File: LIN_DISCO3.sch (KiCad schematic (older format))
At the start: 4 parts

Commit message: schematic: draft
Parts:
- added C1: 100nF, Capacitor_SMD:C_0805_2012Metric_Pad1.15x1.40mm_HandSolder, symbol Device:C
- added C4: CP, Capacitor_SMD:CP_Elec_4x5.8, symbol Device:CP
- added D1, D2: D_Zener_5V6, Diode_SMD:D_0805_2012Metric_Pad1.15x1.40mm_HandSolder, symbol Device:D_Zener
- added D3: LED, LED_SMD:LED_0805_2012Metric_Pad1.15x1.40mm_HandSolder, symbol Device:LED
- added J1: CAR_STAT, TerminalBlock:TerminalBlock_Altech_AK300-2_P5.00mm, symbol Connector:Conn_01x02_Female
- added J2: CAR_BAT, TerminalBlock:TerminalBlock_Altech_AK300-2_P5.00mm, symbol Connector:Conn_01x02_Female
- added J3: WEBASTO, TerminalBlock:TerminalBlock_Altech_AK300-2_P5.00mm, symbol Connector:Conn_01x02_Female
- added R1, R2, R3, R4: 10k, Resistor_SMD:R_0805_2012Metric_Pad1.15x1.40mm_HandSolder, symbol Device:R
- added R5: 2K, Resistor_SMD:R_0805_2012Metric_Pad1.15x1.40mm_HandSolder, symbol Device:R
- added R6: 1K, Resistor_SMD:R_0805_2012Metric_Pad1.15x1.40mm_HandSolder, symbol Device:R
- added U2: MCP1804x-5002xMB, Package_TO_SOT_SMD:SOT-89-3, symbol Regulator_Linear:MCP1804x-5002xMB
- added U3: Si9243A, Package_SO:SOIC-8_3.9x4.9mm_P1.27mm, symbol vishay_Si9243A:Si9243A
- C2, C3: renamed from C?; value C -> 22pF; footprint (none) -> Capacitor_SMD:C_0805_2012Metric_Pad1.15x1.40mm_HandSolder
- Rez1: renamed from Y?; value Crystal -> 18.432MHz; footprint (none) -> Crystal:Crystal_SMD_0603-2Pin_6.0x3.5mm_HandSoldering
- U1: renamed from U?; footprint (none) -> Package_SO:SOIC-18W_7.5x11.6mm_P1.27mm
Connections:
- net GND: now also C1.2, C4.2, D1.2 (A), D2.2 (A), J2.1 (Pin_1), R3.2, R4.2, U2.2 (GND), U3.5 (Gnd)
- net IGNITION: now also D1.1 (K), R2.1, R3.1
- net LOW_BEAM: now also D2.1 (K), R1.1, R4.1
- net Vcc: now also C4.1, U2.1 (OUT), U3.3 (VDD)
- net WLINE_RX: now also U3.1 (RXK)
- net WLINE_TX: now also U3.4 (TX)
- new net: J1.1 (Pin_1), R2.2
- new net: J1.2 (Pin_2), R1.2
- new net: D3.2 (A), R5.1
- new net VBAT: C1.1, J2.2 (Pin_2), R5.2, R6.2, U2.3 (IN), U3.7 (VBAT)
- new net WBUS: D3.1 (K), J3.2 (Pin_2), R6.1, U3.6 (K)
- no-connect marks 0 -> 12

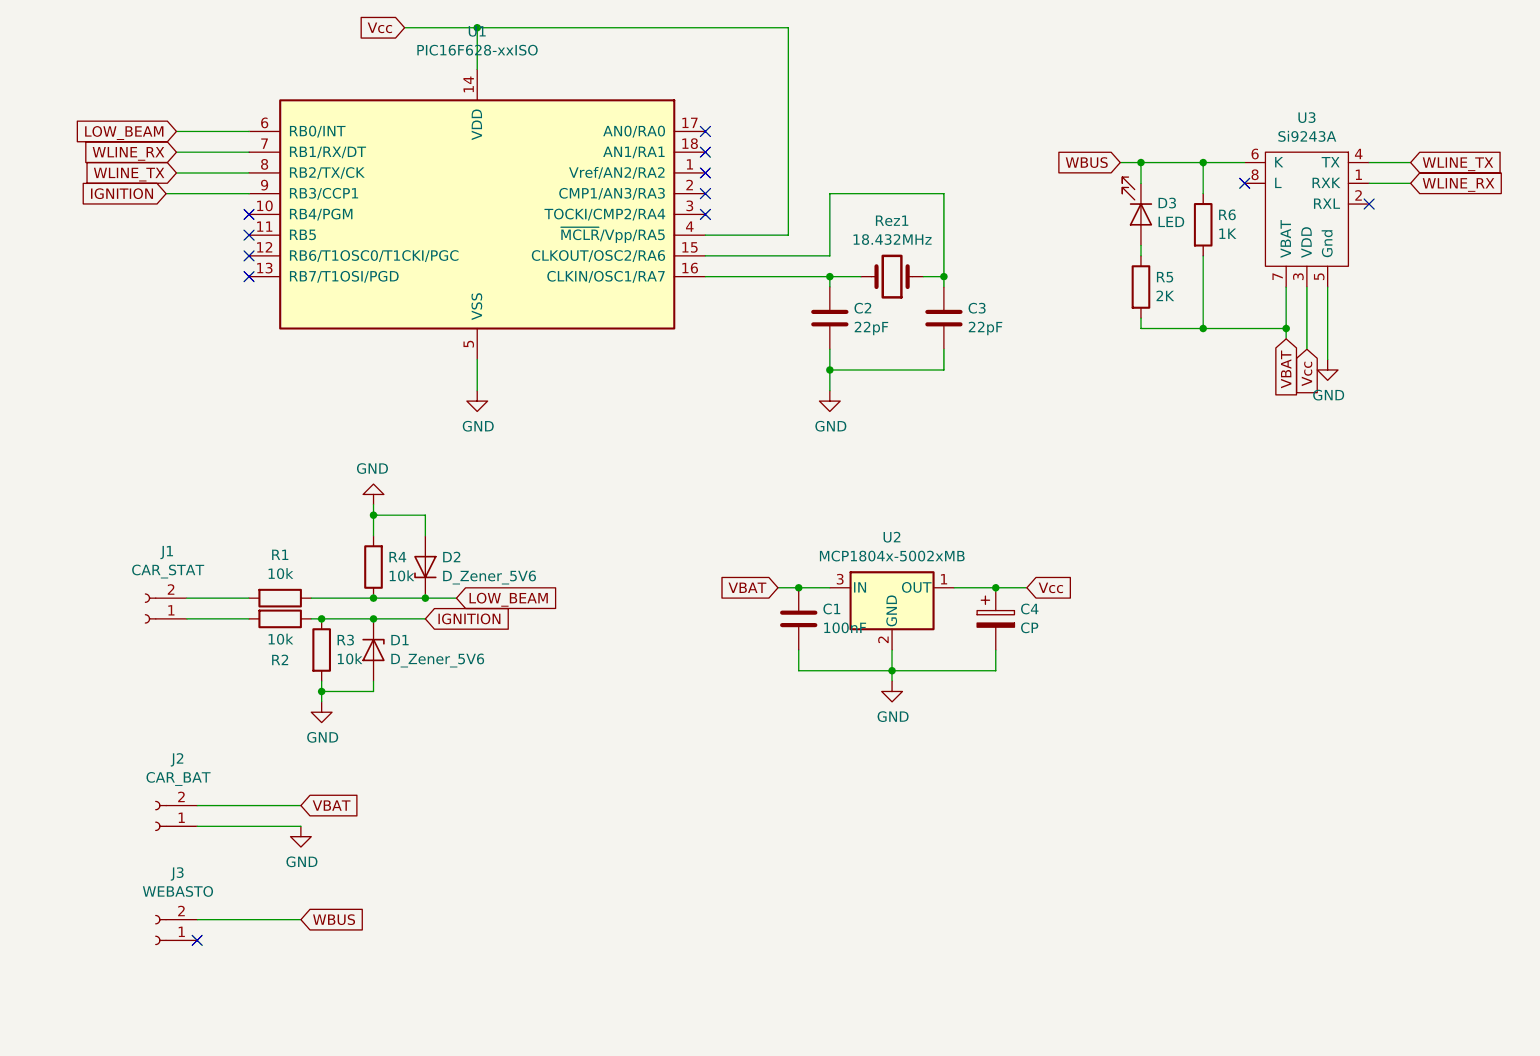
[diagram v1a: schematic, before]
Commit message: reroute, added 6p arks
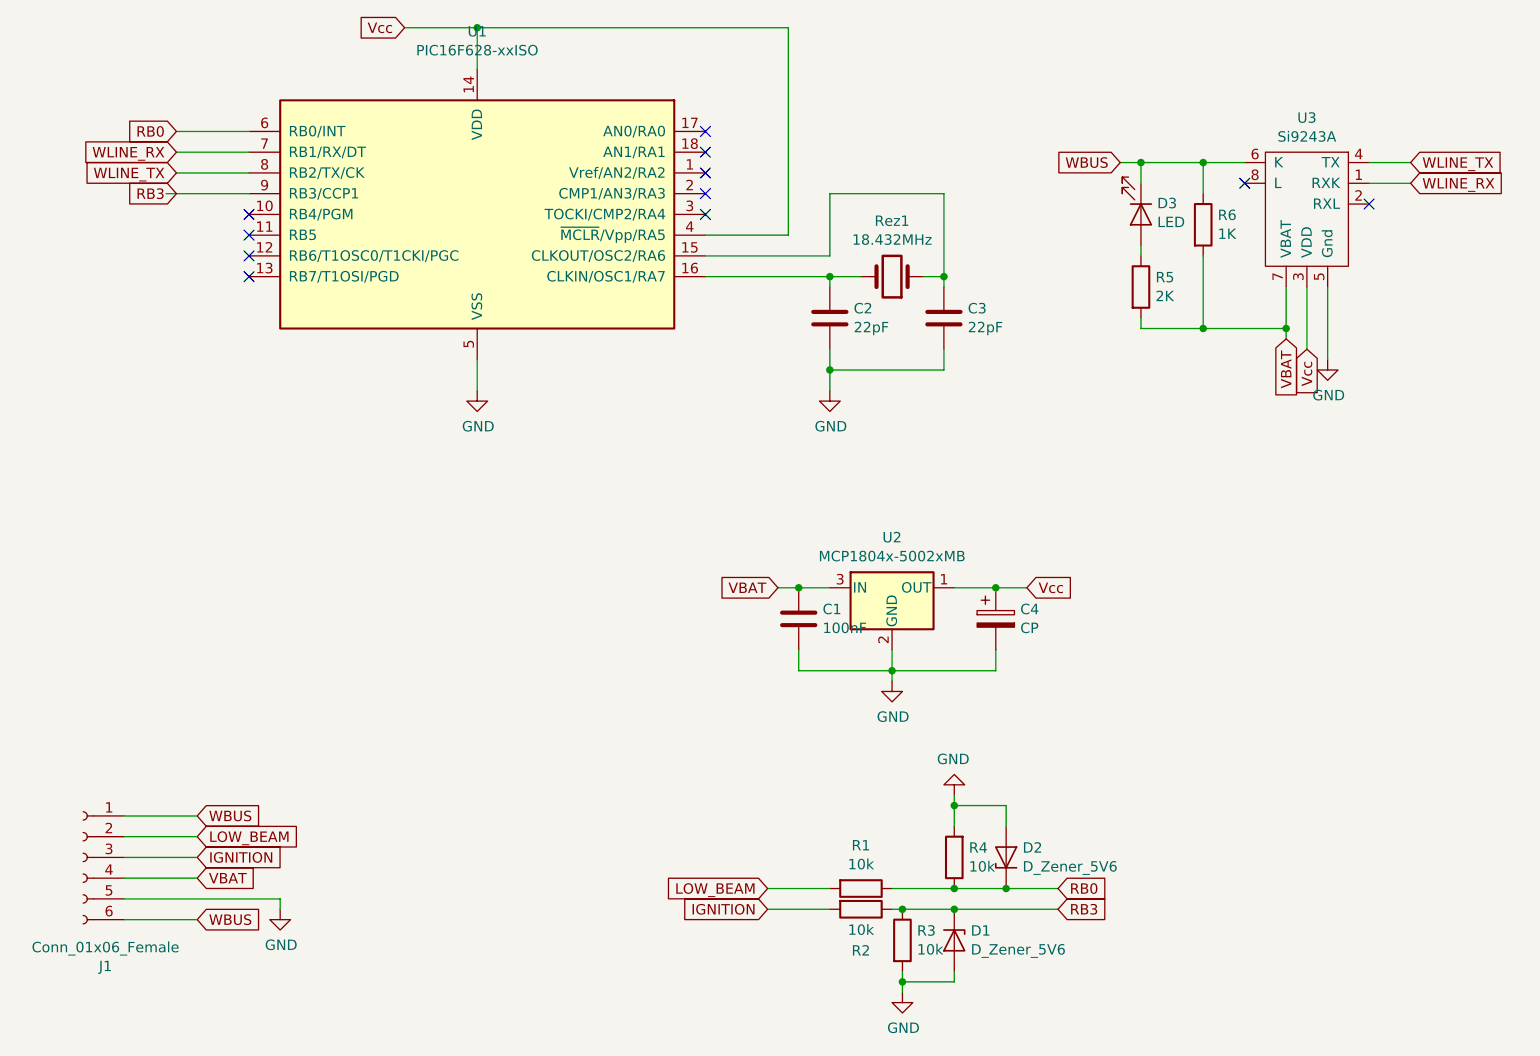
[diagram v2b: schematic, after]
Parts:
- removed J1: CAR_STAT, TerminalBlock:TerminalBlock_Altech_AK300-2_P5.00mm, symbol Connector:Conn_01x02_Female
- removed J2: CAR_BAT, TerminalBlock:TerminalBlock_Altech_AK300-2_P5.00mm, symbol Connector:Conn_01x02_Female
- removed J3: WEBASTO, TerminalBlock:TerminalBlock_Altech_AK300-2_P5.00mm, symbol Connector:Conn_01x02_Female
- added J1: Conn_01x06_Female, TerminalBlock_4Ucon:TerminalBlock_4Ucon_1x06_P3.50mm_Horizontal, symbol Connector:Conn_01x06_Female
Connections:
- net GND: now also J1.5 (Pin_5)
- net IGNITION: now also R2.2, J1.3 (Pin_3); no longer D1.1 (K), R2.1, R3.1, U1.9 (RB3/CCP1)
- net LOW_BEAM: now also R1.2, J1.2 (Pin_2); no longer D2.1 (K), R1.1, R4.1, U1.6 (RB0/INT)
- net VBAT: now also J1.4 (Pin_4)
- net WBUS: now also J1.1 (Pin_1), J1.6 (Pin_6)
- new net RB0: D2.1 (K), R1.1, R4.1, U1.6 (RB0/INT)
- new net RB3: D1.1 (K), R2.1, R3.1, U1.9 (RB3/CCP1)
- no-connect marks 12 -> 11
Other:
- moved on the sheet: D1, D2, R1, R2, R3, R4
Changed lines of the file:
@@
 Wire Wire Line
 	1500 2000 1150 2000
-Text GLabel 1100 2100 0    50   Input ~ 0
-IGNITION
+Text GLabel 1150 2100 0    50   Input ~ 0
+RB3
 Wire Wire Line
 	1100 2100 1500 2100
 Text GLabel 1150 1800 0    50   Input ~ 0
-LOW_BEAM
+RB0
 Wire Wire Line
 	1150 1800 1500 1800
@@
 	6900 1950 7100 1950
 NoConn ~ 6900 2150
-Text GLabel 2350 4150 2    50   Input ~ 0
+Text GLabel 1250 5300 2    50   Input ~ 0
 IGNITION
-Text GLabel 2500 4050 2    50   Input ~ 0
+Text GLabel 1250 5200 2    50   Input ~ 0
 LOW_BEAM
-Wire Wire Line
-	2350 4150 2100 4150
 $Comp
 L Device:R R3
 U 1 1 61F0078F
-P 1850 4300
-F 0 "R3" H 1920 4346 50  0000 L CNN
-F 1 "10k" H 1920 4255 50  0000 L CNN
-F 2 "Resistor_SMD:R_0805_2012Metric_Pad1.15x1.40mm_HandSolder" V 1780 4300 50  0001 C CNN
-F 3 "~" H 1850 4300 50  0001 C CNN
-	1    1850 4300
+P 4650 5700
+F 0 "R3" H 4720 5746 50  0000 L CNN
+F 1 "10k" H 4720 5655 50  0000 L CNN
+F 2 "Resistor_SMD:R_0805_2012Metric_Pad1.15x1.40mm_HandSolder" V 4580 5700 50  0001 C CNN
+F 3 "~" H 4650 5700 50  0001 C CNN
+	1    4650 5700
 	1    0    0    -1
 $EndComp
@@
 L Device:R R4
 U 1 1 61F00BA1
-P 2100 3900
-F 0 "R4" H 2030 3854 50  0000 R CNN
-F 1 "10k" H 2030 3945 50  0000 R CNN
-F 2 "Resistor_SMD:R_0805_2012Metric_Pad1.15x1.40mm_HandSolder" V 2030 3900 50  0001 C CNN
-F 3 "~" H 2100 3900 50  0001 C CNN
-	1    2100 3900
+P 4900 5300
+F 0 "R4" H 4830 5254 50  0000 R CNN
+F 1 "10k" H 4830 5345 50  0000 R CNN
+F 2 "Resistor_SMD:R_0805_2012Metric_Pad1.15x1.40mm_HandSolder" V 4830 5300 50  0001 C CNN
+F 3 "~" H 4900 5300 50  0001 C CNN
+	1    4900 5300
 	-1   0    0    1
 $EndComp
@@
 L Device:D_Zener D2
 U 1 1 61F0371E
-P 2350 3900
-F 0 "D2" V 2396 3821 50  0000 R CNN
-F 1 "D_Zener_5V6" V 2305 3821 50  0000 R CNN
-F 2 "Diode_SMD:D_0805_2012Metric_Pad1.15x1.40mm_HandSolder" H 2350 3900 50  0001 C CNN
-F 3 "~" H 2350 3900 50  0001 C CNN
-	1    2350 3900
+P 5150 5300
+F 0 "D2" V 5196 5221 50  0000 R CNN
+F 1 "D_Zener_5V6" V 5105 5221 50  0000 R CNN
+F 2 "Diode_SMD:D_0805_2012Metric_Pad1.15x1.40mm_HandSolder" H 5150 5300 50  0001 C CNN
+F 3 "~" H 5150 5300 50  0001 C CNN
+	1    5150 5300
 	0    -1   -1   0
 $EndComp
@@
 L Device:D_Zener D1
 U 1 1 61F0512B
-P 2100 4300
-F 0 "D1" V 2054 4379 50  0000 L CNN
-F 1 "D_Zener_5V6" V 2145 4379 50  0000 L CNN
-F 2 "Diode_SMD:D_0805_2012Metric_Pad1.15x1.40mm_HandSolder" H 2100 4300 50  0001 C CNN
-F 3 "~" H 2100 4300 50  0001 C CNN
-	1    2100 4300
+P 4900 5700
+F 0 "D1" V 4854 5779 50  0000 L CNN
+F 1 "D_Zener_5V6" V 4945 5779 50  0000 L CNN
+F 2 "Diode_SMD:D_0805_2012Metric_Pad1.15x1.40mm_HandSolder" H 4900 5700 50  0001 C CNN
+F 3 "~" H 4900 5700 50  0001 C CNN
+	1    4900 5700
 	0    1    1    0
 $EndComp
-Connection ~ 2100 4150
-Wire Wire Line
-	2100 4150 1850 4150
-Connection ~ 2350 4050
-Wire Wire Line
-	2100 4050 2350 4050
-Wire Wire Line
-	2350 4050 2500 4050
+Connection ~ 4900 5550
+Wire Wire Line
+	4900 5550 4650 5550
+Connection ~ 5150 5450
+Wire Wire Line
+	4900 5450 5150 5450
 $Comp
 L power:GND #PWR0104
 U 1 1 61F07EE6
-P 1850 4550
-F 0 "#PWR0104" H 1850 4300 50  0001 C CNN
-F 1 "GND" H 1855 4377 50  0000 C CNN
-F 2 "" H 1850 4550 50  0001 C CNN
-F 3 "" H 1850 4550 50  0001 C CNN
-	1    1850 4550
-	1    0    0    -1
-$EndComp
-Wire Wire Line
-	1850 4550 1850 4500
-Wire Wire Line
-	1850 4500 2100 4500
-Wire Wire Line
-	2100 4500 2100 4450
-Connection ~ 1850 4500
-Wire Wire Line
-	1850 4500 1850 4450
+P 4650 5950
+F 0 "#PWR0104" H 4650 5700 50  0001 C CNN
+F 1 "GND" H 4655 5777 50  0000 C CNN
+F 2 "" H 4650 5950 50  0001 C CNN
+F 3 "" H 4650 5950 50  0001 C CNN
+	1    4650 5950
+	1    0    0    -1
+$EndComp
+Wire Wire Line
+	4650 5950 4650 5900
+Wire Wire Line
+	4650 5900 4900 5900
+Wire Wire Line
+	4900 5900 4900 5850
+Connection ~ 4650 5900
+Wire Wire Line
+	4650 5900 4650 5850
 $Comp
 L power:GND #PWR0105
 U 1 1 61F0907F
-P 2100 3600
-F 0 "#PWR0105" H 2100 3350 50  0001 C CNN
-F 1 "GND" H 2105 3427 50  0000 C CNN
-F 2 "" H 2100 3600 50  0001 C CNN
-F 3 "" H 2100 3600 50  0001 C CNN
-	1    2100 3600
+P 4900 5000
+F 0 "#PWR0105" H 4900 4750 50  0001 C CNN
+F 1 "GND" H 4905 4827 50  0000 C CNN
+F 2 "" H 4900 5000 50  0001 C CNN
+F 3 "" H 4900 5000 50  0001 C CNN
+	1    4900 5000
 	-1   0    0    1
 $EndComp
 Wire Wire Line
-	2100 3600 2100 3650
-Wire Wire Line
-	2100 3650 2350 3650
-Wire Wire Line
-	2350 3650 2350 3750
-Connection ~ 2100 3650
-Wire Wire Line
-	2100 3650 2100 3750
+	4900 5000 4900 5050
+Wire Wire Line
+	4900 5050 5150 5050
+Wire Wire Line
+	5150 5050 5150 5150
+Connection ~ 4900 5050
+Wire Wire Line
+	4900 5050 4900 5150
 $Comp
 L Device:R R1
 U 1 1 61F0D0F3
-P 1650 4050
-F 0 "R1" V 1443 4050 50  0000 C CNN
-F 1 "10k" V 1534 4050 50  0000 C CNN
-F 2 "Resistor_SMD:R_0805_2012Metric_Pad1.15x1.40mm_HandSolder" V 1580 4050 50  0001 C CNN
-F 3 "~" H 1650 4050 50  0001 C CNN
-	1    1650 4050
+P 4450 5450
+F 0 "R1" V 4243 5450 50  0000 C CNN
+F 1 "10k" V 4334 5450 50  0000 C CNN
+F 2 "Resistor_SMD:R_0805_2012Metric_Pad1.15x1.40mm_HandSolder" V 4380 5450 50  0001 C CNN
+F 3 "~" H 4450 5450 50  0001 C CNN
+	1    4450 5450
 	0    1    1    0
 $EndComp
@@
 L Device:R R2
 U 1 1 61F0D479
-P 1650 4150
-F 0 "R2" V 1850 4150 50  0000 C CNN
-F 1 "10k" V 1750 4150 50  0000 C CNN
-F 2 "Resistor_SMD:R_0805_2012Metric_Pad1.15x1.40mm_HandSolder" V 1580 4150 50  0001 C CNN
-F 3 "~" H 1650 4150 50  0001 C CNN
-	1    1650 4150
+P 4450 5550
+F 0 "R2" V 4650 5550 50  0000 C CNN
+F 1 "10k" V 4550 5550 50  0000 C CNN
+F 2 "Resistor_SMD:R_0805_2012Metric_Pad1.15x1.40mm_HandSolder" V 4380 5550 50  0001 C CNN
+F 3 "~" H 4450 5550 50  0001 C CNN
+	1    4450 5550
 	0    1    1    0
 $EndComp
 Wire Wire Line
-	1800 4150 1850 4150
-Connection ~ 1850 4150
-Wire Wire Line
-	1800 4050 2100 4050
-Connection ~ 2100 4050
-Wire Wire Line
-	1500 4050 1200 4050
-Wire Wire Line
-	1200 4150 1500 4150
+	4600 5550 4650 5550
+Connection ~ 4650 5550
+Wire Wire Line
+	4600 5450 4900 5450
+Connection ~ 4900 5450
+Wire Wire Line
+	4300 5450 4000 5450
+Wire Wire Line
+	4000 5550 4300 5550
 $Comp
 L Regulator_Linear:MCP1804x-5002xMB U2
@@
 	5800 2700 5800 2750
 $Comp
-L Connector:Conn_01x02_Female J2
-U 1 1 61F3300B
-P 1050 5150
-F 0 "J2" H 942 4825 50  0000 C CNN
-F 1 "CAR_BAT" H 942 4916 50  0000 C CNN
-F 2 "TerminalBlock:TerminalBlock_Altech_AK300-2_P5.00mm" H 1050 5150 50  0001 C CNN
-F 3 "~" H 1050 5150 50  0001 C CNN
-	1    1050 5150
-	-1   0    0    1
-$EndComp
-$Comp
 L power:GND #PWR0107
 U 1 1 61F39679
-P 1750 5150
-F 0 "#PWR0107" H 1750 4900 50  0001 C CNN
-F 1 "GND" H 1755 4977 50  0000 C CNN
-F 2 "" H 1750 5150 50  0001 C CNN
-F 3 "" H 1750 5150 50  0001 C CNN
-	1    1750 5150
-	1    0    0    -1
-$EndComp
-Wire Wire Line
-	1250 5150 1750 5150
-Text GLabel 1750 5050 2    50   Input ~ 0
+P 1650 5550
+F 0 "#PWR0107" H 1650 5300 50  0001 C CNN
+F 1 "GND" H 1655 5377 50  0000 C CNN
+F 2 "" H 1650 5550 50  0001 C CNN
+F 3 "" H 1650 5550 50  0001 C CNN
+	1    1650 5550
+	1    0    0    -1
+$EndComp
+Text GLabel 1250 5400 2    50   Input ~ 0
 VBAT
-Wire Wire Line
-	1250 5050 1750 5050
-$Comp
-L Connector:Conn_01x02_Female J1
-U 1 1 61EFD6D9
-P 1000 4150
-F 0 "J1" H 892 3825 50  0000 C CNN
-F 1 "CAR_STAT" H 892 3916 50  0000 C CNN
-F 2 "TerminalBlock:TerminalBlock_Altech_AK300-2_P5.00mm" H 1000 4150 50  0001 C CNN
-F 3 "~" H 1000 4150 50  0001 C CNN
-	1    1000 4150
-	-1   0    0    1
-$EndComp
-$Comp
-L Connector:Conn_01x02_Female J3
-U 1 1 61EF80E6
-P 1050 5700
-F 0 "J3" H 942 5375 50  0000 C CNN
-F 1 "WEBASTO" H 942 5466 50  0000 C CNN
-F 2 "TerminalBlock:TerminalBlock_Altech_AK300-2_P5.00mm" H 1050 5700 50  0001 C CNN
-F 3 "~" H 1050 5700 50  0001 C CNN
-	1    1050 5700
-	-1   0    0    1
-$EndComp
-Text GLabel 1750 5600 2    50   Input ~ 0
+Text GLabel 1250 5600 2    50   Input ~ 0
 WBUS
-Wire Wire Line
-	1250 5600 1750 5600
-NoConn ~ 1250 5700
+Text GLabel 4000 5450 0    50   Input ~ 0
+LOW_BEAM
+Text GLabel 4000 5550 0    50   Input ~ 0
+IGNITION
+Text GLabel 5400 5550 2    50   Input ~ 0
+RB3
+Wire Wire Line
+	4900 5550 5400 5550
+Text GLabel 5400 5450 2    50   Input ~ 0
+RB0
+Wire Wire Line
+	5150 5450 5400 5450
+$Comp
+L Connector:Conn_01x06_Female J1
+U 1 1 61F6A2D8
+P 700 5300
+F 0 "J1" H 592 4775 50  0000 C CNN
+F 1 "Conn_01x06_Female" H 592 4866 50  0000 C CNN
+F 2 "TerminalBlock_4Ucon:TerminalBlock_4Ucon_1x06_P3.50mm_Horizontal" H 700 5300 50  0001 C CNN
+F 3 "~" H 700 5300 50  0001 C CNN
+	1    700  5300
+	-1   0    0    -1
+$EndComp
+Text GLabel 1250 5100 2    50   Input ~ 0
+WBUS
+Wire Wire Line
+	1250 5400 900  5400
+Wire Wire Line
+	900  5600 1250 5600
+Wire Wire Line
+	1250 5300 900  5300
+Wire Wire Line
+	900  5200 1250 5200
+Wire Wire Line
+	900  5100 1250 5100
+Wire Wire Line
+	1650 5500 1650 5550
+Wire Wire Line
+	900  5500 1650 5500
 $EndSCHEMATC
